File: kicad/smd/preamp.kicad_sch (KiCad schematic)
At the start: 18 parts, among them Q1 MMBF5457, Q2 MMBF5457

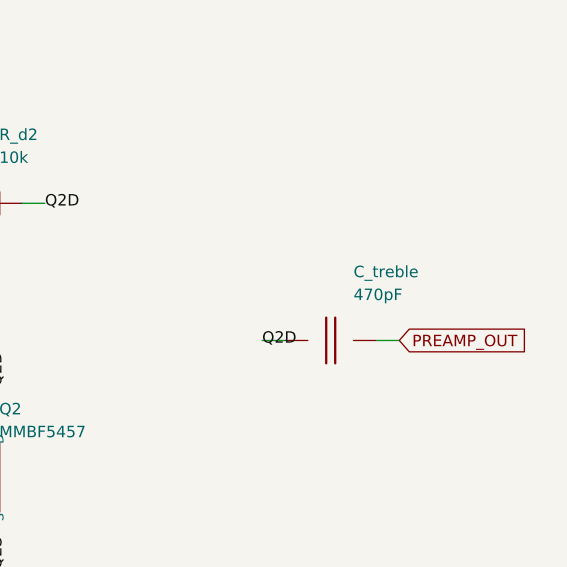
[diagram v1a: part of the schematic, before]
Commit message: Tone stack: Bass + Treble (passive James) with a switchable mid cut (errata #20)
The panel has Bass and Treble pots, but the design carried a single treble-cut
"Tone" substitute -- and the recovered preamp coupling was the 470 pF chime cap
alone, a 1.3 kHz high-pass that passed no bass at all. Replace both:

- C_cpl_out 1 uF full-band coupling from Q2's drain; C_treble 470 pF becomes a
  bright cap across the top of the volume pot.
- Passive James (Thomas-Vox) Bass/Treble network -- the originals' topology,
  asymmetric, more cut than boost, kept over an active Baxandall so the amp
  keeps its character -- driven by a TL074 (IC3: input buffer, x2 make-up,
  gyrator, output buffer) on its own mid-rail VBIAS_3. Both pots 250k lin in
  the original holes.
- MID CUT toggle for honky pickups: R_mid + a switched series-resonant gyrator
  shunt (1.86 H simulated + 22 nF): -9.6 dB at ~800 Hz, Q ~0.6, flat when off,
  no DC across the switch. SW_MID sits in the original line-reverse switch
  hole -- no new panel holes.
- SPICE: ac_tonestack.cir rewritten rail-aware (all IC3 nodes 8.50 V, noon
  -0.21 dB, notch -9.65 dB at 796 Hz); sweep_tonestack.cir sweeps both pots
  and the switch; results committed.

Generator / placer / router:
- OPAMP14 and SW_SPST symbols, VB_3 / TMK test points (28), BOM rows for IC3,
  the DIP-14 socket, POT_BASS/POT_TREB, SW_MID.
- gen_pcb: tighter profiles (THT 1.2 mm gap / 3.5 mm channels, SMD 0.4 mm),
  overflow repair by moving width between columns, small parts kept in
  schematic order on the shelves, tone/preamp column weighted wider, TP cells
  6x4.5 with the courtyard flush to the cell, input-jack pads down the LEFT
  edge on the 155x90 board (the bottom edge is ~9 mm short for 13 groups),
  keepout rule areas (2 mm edge frame + M3 hole squares) exported to the
  router.
- route_board: refuse a board without its .kicad_pro (a copy routed away from
  the project came back with 0.2 mm tracks and 400 DRC errors); prune
  zero-length segments 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
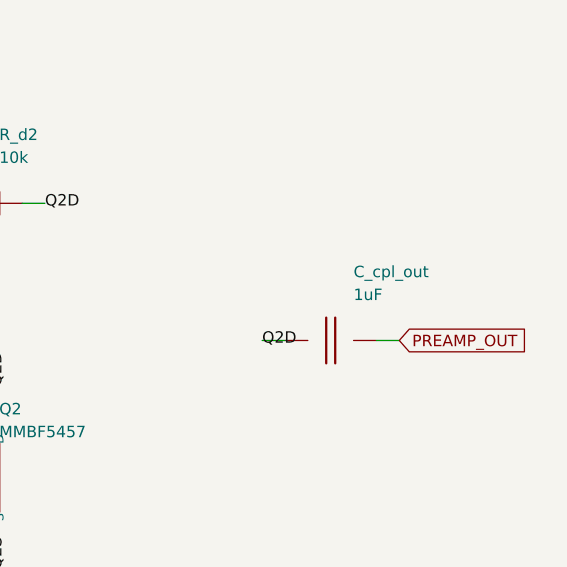
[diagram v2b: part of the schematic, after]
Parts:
- removed C_treble: 470pF, Capacitor_SMD:C_1206_3216Metric, symbol cr_primitives:C
- added C_cpl_out: 1uF, Capacitor_SMD:C_1210_3225Metric, symbol cr_primitives:C
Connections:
- net PREAMP_OUT: now also C_cpl_out.2
- net Q2D: now also C_cpl_out.1
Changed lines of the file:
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@@
     (pin "1")
     (pin "2")
-    (instances (project "cambridge_reverb" (path "/902fcf43-5cb1-4e8b-b98f-8468251a6c1d" (reference "C_in_pre") (unit 1))))
+    (instances (project "cambridge_reverb" (path "/5b84e5e5-91b6-42b0-88cf-3f1bb701d156" (reference "C_in_pre") (unit 1))))
   )
   (wire (pts (xy 116.84 53.339999999999996) (xy 114.3 53.339999999999996)) (stroke (width 0) (type default)))
@@
     (pin "1")
     (pin "2")
-    (instances (project "cambridge_reverb" (path "/902fcf43-5cb1-4e8b-b98f-8468251a6c1d" (reference "R_g1") (unit 1))))
+    (instances (project "cambridge_reverb" (path "/5b84e5e5-91b6-42b0-88cf-3f1bb701d156" (reference "R_g1") (unit 1))))
   )
   (wire (pts (xy 116.84 83.82000000000001) (xy 114.3 83.82000000000001)) (stroke (width 0) (type default)))
@@
     (pin "1")
     (pin "2")
-    (instances (project "cambridge_reverb" (path "/902fcf43-5cb1-4e8b-b98f-8468251a6c1d" (reference "Q1") (unit 1))))
+    (instances (project "cambridge_reverb" (path "/5b84e5e5-91b6-42b0-88cf-3f1bb701d156" (reference "Q1") (unit 1))))
   )
   (wire (pts (xy 165.1 63.49999999999999) (xy 162.56 63.49999999999999)) (stroke (width 0) (type default)))
@@
     (pin "1")
     (pin "2")
-    (instances (project "cambridge_reverb" (path "/902fcf43-5cb1-4e8b-b98f-8468251a6c1d" (reference "R_d1") (unit 1))))
+    (instances (project "cambridge_reverb" (path "/5b84e5e5-91b6-42b0-88cf-3f1bb701d156" (reference "R_d1") (unit 1))))
   )
   (wire (pts (xy 167.64 33.019999999999996) (xy 165.1 33.019999999999996)) (stroke (width 0) (type default)))
@@
     (pin "1")
     (pin "2")
-    (instances (project "cambridge_reverb" (path "/902fcf43-5cb1-4e8b-b98f-8468251a6c1d" (reference "R_s1") (unit 1))))
+    (instances (project "cambridge_reverb" (path "/5b84e5e5-91b6-42b0-88cf-3f1bb701d156" (reference "R_s1") (unit 1))))
   )
   (wire (pts (xy 167.64 104.14) (xy 165.1 104.14)) (stroke (width 0) (type default)))
@@
     (pin "1")
     (pin "2")
-    (instances (project "cambridge_reverb" (path "/902fcf43-5cb1-4e8b-b98f-8468251a6c1d" (reference "C_s1") (unit 1))))
+    (instances (project "cambridge_reverb" (path "/5b84e5e5-91b6-42b0-88cf-3f1bb701d156" (reference "C_s1") (unit 1))))
   )
   (wire (pts (xy 207.01 104.14) (xy 204.46999999999997 104.14)) (stroke (width 0) (type default)))
@@
     (pin "1")
     (pin "2")
-    (instances (project "cambridge_reverb" (path "/902fcf43-5cb1-4e8b-b98f-8468251a6c1d" (reference "C_cpl12") (unit 1))))
+    (instances (project "cambridge_reverb" (path "/5b84e5e5-91b6-42b0-88cf-3f1bb701d156" (reference "C_cpl12") (unit 1))))
   )
   (wire (pts (xy 207.01 63.49999999999999) (xy 204.46999999999997 63.49999999999999)) (stroke (width 0) (type default)))
@@
     (pin "1")
     (pin "2")
-    (instances (project "cambridge_reverb" (path "/902fcf43-5cb1-4e8b-b98f-8468251a6c1d" (reference "R_g2") (unit 1))))
+    (instances (project "cambridge_reverb" (path "/5b84e5e5-91b6-42b0-88cf-3f1bb701d156" (reference "R_g2") (unit 1))))
   )
   (wire (pts (xy 207.01 88.9) (xy 204.46999999999997 88.9)) (stroke (width 0) (type default)))
@@
     (pin "1")
     (pin "2")
-    (instances (project "cambridge_reverb" (path "/902fcf43-5cb1-4e8b-b98f-8468251a6c1d" (reference "Q2") (unit 1))))
+    (instances (project "cambridge_reverb" (path "/5b84e5e5-91b6-42b0-88cf-3f1bb701d156" (reference "Q2") (unit 1))))
   )
   (wire (pts (xy 250.19 63.49999999999999) (xy 247.64999999999998 63.49999999999999)) (stroke (width 0) (type default)))
@@
     (pin "1")
     (pin "2")
-    (instances (project "cambridge_reverb" (path "/902fcf43-5cb1-4e8b-b98f-8468251a6c1d" (reference "R_d2") (unit 1))))
+    (instances (project "cambridge_reverb" (path "/5b84e5e5-91b6-42b0-88cf-3f1bb701d156" (reference "R_d2") (unit 1))))
   )
   (wire (pts (xy 252.72999999999996 33.019999999999996) (xy 250.19 33.019999999999996)) (stroke (width 0) (type default)))
@@
     (pin "1")
     (pin "2")
-    (instances (project "cambridge_reverb" (path "/902fcf43-5cb1-4e8b-b98f-8468251a6c1d" (reference "C_pres") (unit 1))))
+    (instances (project "cambridge_reverb" (path "/5b84e5e5-91b6-42b0-88cf-3f1bb701d156" (reference "C_pres") (unit 1))))
   )
   (wire (pts (xy 252.72999999999996 104.14) (xy 250.19 104.14)) (stroke (width 0) (type default)))
@@
     (pin "1")
     (pin "2")
-    (instances (project "cambridge_reverb" (path "/902fcf43-5cb1-4e8b-b98f-8468251a6c1d" (reference "R_s2") (unit 1))))
+    (instances (project "cambridge_reverb" (path "/5b84e5e5-91b6-42b0-88cf-3f1bb701d156" (reference "R_s2") (unit 1))))
   )
   (wire (pts (xy 292.09999999999997 88.9) (xy 289.56 88.9)) (stroke (width 0) (type default)))
@@
     (pin "1")
     (pin "2")
-    (instances (project "cambridge_reverb" (path "/902fcf43-5cb1-4e8b-b98f-8468251a6c1d" (reference "C_s2") (unit 1))))
+    (instances (project "cambridge_reverb" (path "/5b84e5e5-91b6-42b0-88cf-3f1bb701d156" (reference "C_s2") (unit 1))))
   )
   (wire (pts (xy 292.09999999999997 113.03) (xy 289.56 113.03)) (stroke (width 0) (type default)))
@@
   (symbol (lib_id "cr_primitives:C") (at 297.18 48.26 0) (unit 1)
     (in_bom yes) (on_board yes) (dnp no)
-    (property "Reference" "C_treble" (at 299.72 40.64 0) (effects (font (size 1.27 1.27)) (justify left)))
-    (property "Value" "470pF" (at 299.72 43.18 0) (effects (font (size 1.27 1.27)) (justify left)))
-    (property "Footprint" "Capacitor_SMD:C_1206_3216Metric" (at 297.18 48.26 0) (effects (font (size 1.27 1.27)) hide))
-    (pin "1")
-    (pin "2")
-    (instances (project "cambridge_reverb" (path "/902fcf43-5cb1-4e8b-b98f-8468251a6c1d" (reference "C_treble") (unit 1))))
+    (property "Reference" "C_cpl_out" (at 299.72 40.64 0) (effects (font (size 1.27 1.27)) (justify left)))
+    (property "Value" "1uF" (at 299.72 43.18 0) (effects (font (size 1.27 1.27)) (justify left)))
+    (property "Footprint" "Capacitor_SMD:C_1210_3225Metric" (at 297.18 48.26 0) (effects (font (size 1.27 1.27)) hide))
+    (pin "1")
+    (pin "2")
+    (instances (project "cambridge_reverb" (path "/5b84e5e5-91b6-42b0-88cf-3f1bb701d156" (reference "C_cpl_out") (unit 1))))
   )
   (wire (pts (xy 292.09999999999997 48.26) (xy 289.56 48.26)) (stroke (width 0) (type default)))
@@
     (property "Footprint" "cambridge_reverb:TestPoint_THT_D2.0mm_Label" (at 121.91999999999999 243.84 0) (effects (font (size 1.27 1.27)) hide))
     (pin "1")
-    (instances (project "cambridge_reverb" (path "/902fcf43-5cb1-4e8b-b98f-8468251a6c1d" (reference "TP_Q1D") (unit 1))))
+    (instances (project "cambridge_reverb" (path "/5b84e5e5-91b6-42b0-88cf-3f1bb701d156" (reference "TP_Q1D") (unit 1))))
   )
   (wire (pts (xy 121.91999999999999 246.38) (xy 121.91999999999999 248.92)) (stroke (width 0) (type default)))
@@
     (property "Footprint" "cambridge_reverb:TestPoint_THT_D2.0mm_Label" (at 147.32 243.84 0) (effects (font (size 1.27 1.27)) hide))
     (pin "1")
-    (instances (project "cambridge_reverb" (path "/902fcf43-5cb1-4e8b-b98f-8468251a6c1d" (reference "TP_Q2D") (unit 1))))
+    (instances (project "cambridge_reverb" (path "/5b84e5e5-91b6-42b0-88cf-3f1bb701d156" (reference "TP_Q2D") (unit 1))))
   )
   (wire (pts (xy 147.32 246.38) (xy 147.32 248.92)) (stroke (width 0) (type default)))
@@
     (property "Footprint" "cambridge_reverb:TestPoint_THT_D2.0mm_Label" (at 172.72 243.84 0) (effects (font (size 1.27 1.27)) hide))
     (pin "1")
-    (instances (project "cambridge_reverb" (path "/902fcf43-5cb1-4e8b-b98f-8468251a6c1d" (reference "TP_PRE_OUT") (unit 1))))
+    (instances (project "cambridge_reverb" (path "/5b84e5e5-91b6-42b0-88cf-3f1bb701d156" (reference "TP_PRE_OUT") (unit 1))))
   )
   (wire (pts (xy 172.72 246.38) (xy 172.72 248.92)) (stroke (width 0) (type default)))
@@
     (property "Footprint" "cambridge_reverb:TestPoint_THT_D2.0mm_Label" (at 198.12 243.84 0) (effects (font (size 1.27 1.27)) hide))
     (pin "1")
-    (instances (project "cambridge_reverb" (path "/902fcf43-5cb1-4e8b-b98f-8468251a6c1d" (reference "TP_GND_PRE") (unit 1))))
+    (instances (project "cambridge_reverb" (path "/5b84e5e5-91b6-42b0-88cf-3f1bb701d156" (reference "TP_GND_PRE") (unit 1))))
   )
   (wire (pts (xy 198.12 246.38) (xy 198.12 248.92)) (stroke (width 0) (type default)))
